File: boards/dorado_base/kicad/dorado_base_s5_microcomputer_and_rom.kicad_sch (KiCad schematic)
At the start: 11 parts

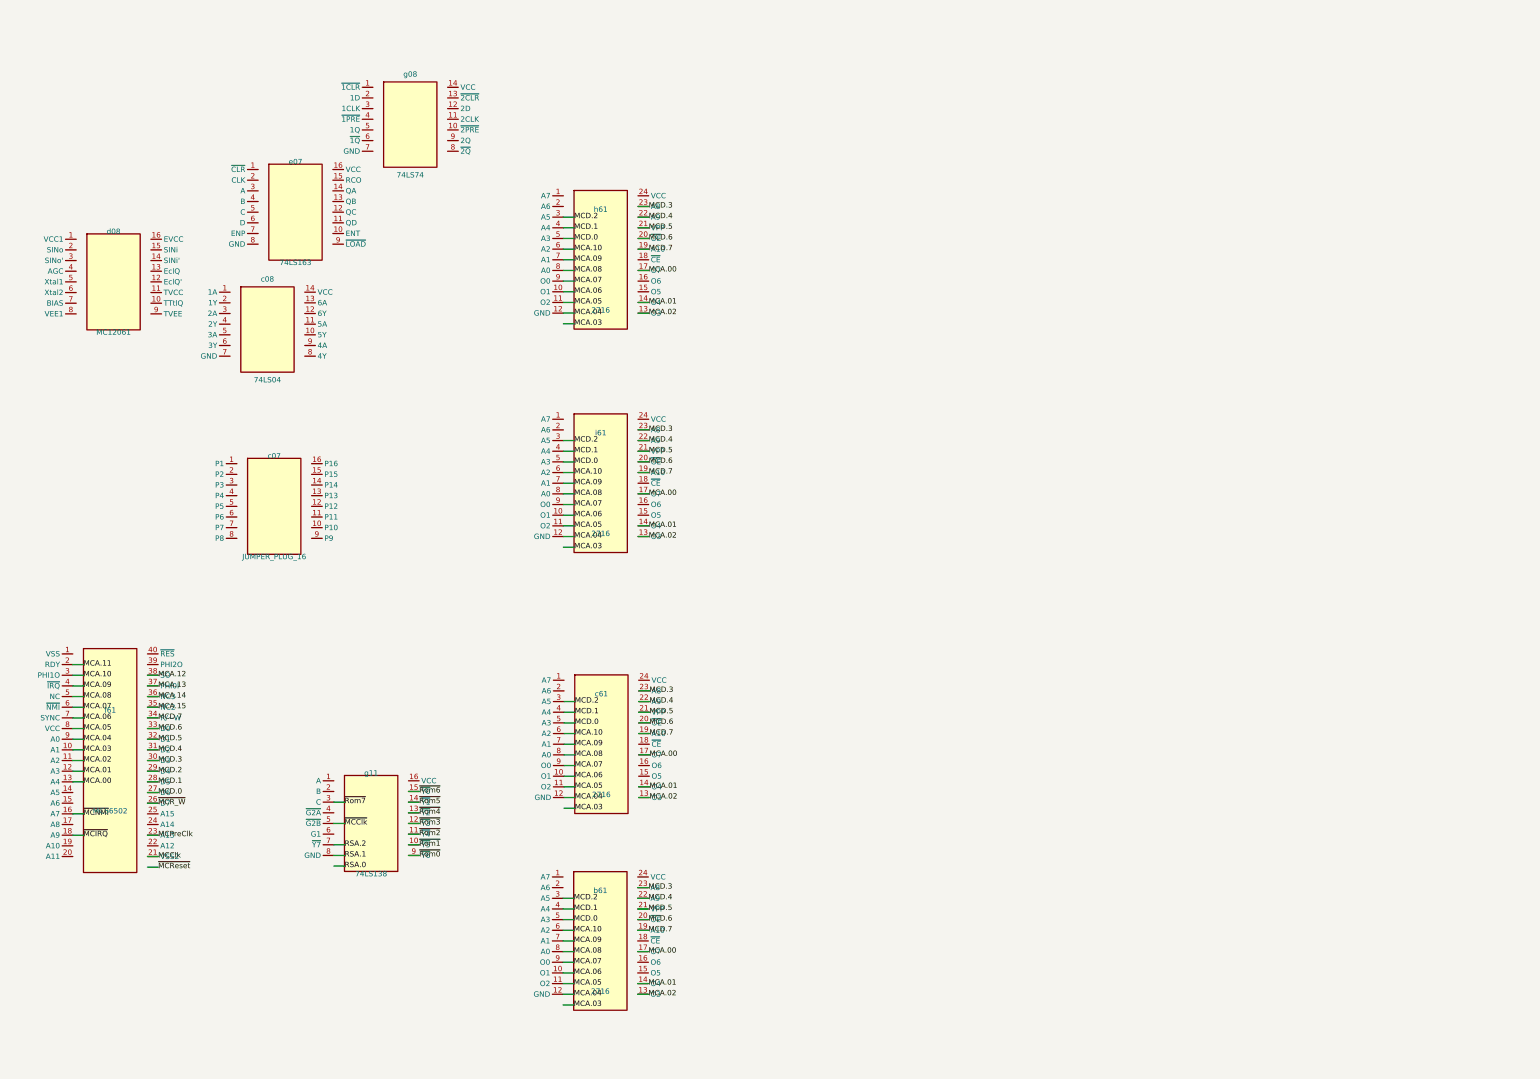
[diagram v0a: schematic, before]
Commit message: Harness improvements: split-gate exporter, extend-net, board ERC roll-up, on-demand PDF rendering
- kicad_export: emit per-sub-unit lib_symbols (e.g. MC10124_a/b/c/d) sized
  to each gate's pin set; sub-unit detection is graph-evidenced so chips
  with letter-named functional groups (74LS245 A/B) stay single-unit.
  Eliminates phantom pin_to_pin/multiple_net_names ERC errors on split-gate
  sheets and makes each gate render with only its own pins.

- explorer: defaultPinPositions filters to the active gate's pins for
  sub-unit refdes; mirrors kicad_export's predicate. getPinSourcePos now
  requires the component's sheet to match the current view, so endpoints
  with stale/missing sheet fields can't paint stray wires on undecoded
  pages. Also patched 11 such endpoints in dorado_base/graph.json.

- graph_cli: new extend-net verb appends endpoints to an existing net
  (errors on unknown net or edge_type mismatch, skips duplicates).
  erc-summary --board <id> aggregates every sheet's report and surfaces
  named labels with only one endpoint across the whole board — the real
  off-page connections still missing.

- cartographer: tile and crop-chip accept --pdf <path> --page <n>
  --dpi <n> to render fresh from the source PDF on demand. crop-chip
  auto-rescales the bbox by render-vs-scan size ratio so a 600 DPI crop
  still frames the chip from a graph populated against 300 DPI scans.

Co-Authored-By: Claude Opus 4.7 (1M context) <noreply@anthropic.com>
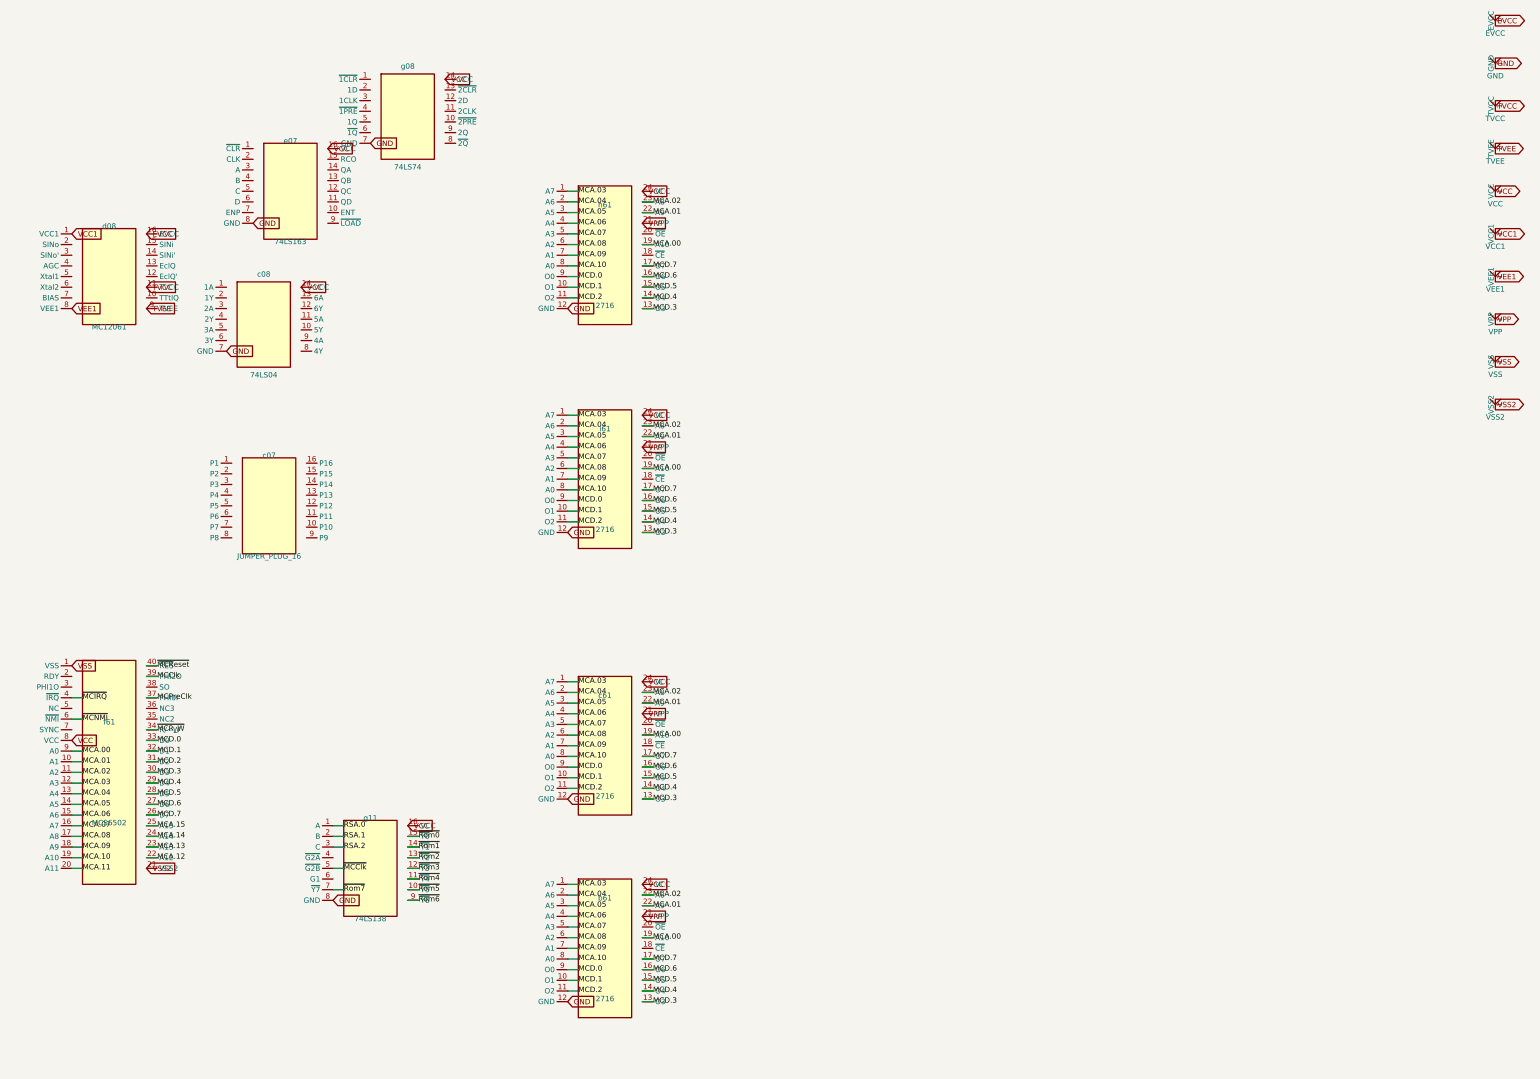
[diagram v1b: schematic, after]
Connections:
- net MCA.00: now also b61.19 (A10), c61.19 (A10), f61.9 (A0), h61.19 (A10), i61.19 (A10); no longer b61.17 (O7), c61.17 (O7), f61.13 (A4), h61.17 (O7), i61.17 (O7)
- net MCA.01: now also b61.22 (A9), c61.22 (A9), f61.10 (A1), h61.22 (A9), i61.22 (A9); no longer b61.14 (O4), c61.14 (O4), f61.12 (A3), h61.14 (O4), i61.14 (O4)
- net MCA.02: now also b61.23 (A8), c61.23 (A8), h61.23 (A8), i61.23 (A8); no longer b61.13 (O3), c61.13 (O3), h61.13 (O3), i61.13 (O3)
- net MCA.03: now also b61.1 (A7), c61.1 (A7), f61.12 (A3), h61.1 (A7), i61.1 (A7); no longer f61.10 (A1)
- net MCA.04: now also b61.2 (A6), c61.2 (A6), f61.13 (A4), h61.2 (A6), i61.2 (A6); no longer b61.12 (GND), c61.12 (GND), f61.9 (A0), h61.12 (GND), i61.12 (GND)
- net MCA.05: now also b61.3 (A5), c61.3 (A5), f61.14 (A5), h61.3 (A5), i61.3 (A5); no longer b61.11 (O2), c61.11 (O2), f61.8 (VCC), h61.11 (O2), i61.11 (O2)
- net MCA.06: now also b61.4 (A4), c61.4 (A4), f61.15 (A6), h61.4 (A4), i61.4 (A4); no longer b61.10 (O1), c61.10 (O1), f61.7 (SYNC), h61.10 (O1), i61.10 (O1)
- net MCA.07: now also b61.5 (A3), c61.5 (A3), f61.16 (A7), h61.5 (A3), i61.5 (A3); no longer b61.9 (O0), c61.9 (O0), f61.6 (~{NMI}), h61.9 (O0), i61.9 (O0)
- net MCA.08: now also b61.6 (A2), c61.6 (A2), f61.17 (A8), h61.6 (A2), i61.6 (A2); no longer b61.8 (A0), c61.8 (A0), f61.5 (NC), h61.8 (A0), i61.8 (A0)
- net MCA.09: now also f61.18 (A9); no longer f61.4 (~{IRQ})
- net MCA.10: now also b61.8 (A0), c61.8 (A0), f61.19 (A10), h61.8 (A0), i61.8 (A0); no longer b61.6 (A2), c61.6 (A2), f61.3 (PHI1O), h61.6 (A2), i61.6 (A2)
- net MCA.11: now also f61.20 (A11); no longer f61.2 (RDY)
- net MCA.12: now also f61.22 (A12); no longer f61.38 (SO)
- net MCA.13: now also f61.23 (A13); no longer f61.37 (PHI0I)
- net MCA.14: now also f61.24 (A14); no longer f61.36 (NC3)
- net MCA.15: now also f61.25 (A15); no longer f61.35 (NC2)
- net MCClk: now also f61.39 (PHI2O); no longer f61.21 (VSS2)
- net MCD.0: now also b61.9 (O0), c61.9 (O0), f61.33 (D0), h61.9 (O0), i61.9 (O0); no longer b61.5 (A3), c61.5 (A3), f61.27 (D6), h61.5 (A3), i61.5 (A3)
- net MCD.1: now also b61.10 (O1), c61.10 (O1), f61.32 (D1), h61.10 (O1), i61.10 (O1); no longer b61.4 (A4), c61.4 (A4), f61.28 (D5), h61.4 (A4), i61.4 (A4)
- net MCD.2: now also b61.11 (O2), c61.11 (O2), f61.31 (D2), h61.11 (O2), i61.11 (O2); no longer b61.3 (A5), c61.3 (A5), f61.29 (D4), h61.3 (A5), i61.3 (A5)
- net MCD.3: now also b61.13 (O3), c61.13 (O3), h61.13 (O3), i61.13 (O3); no longer b61.23 (A8), c61.23 (A8), h61.23 (A8), i61.23 (A8)
- net MCD.4: now also b61.14 (O4), c61.14 (O4), f61.29 (D4), h61.14 (O4), i61.14 (O4); no longer b61.22 (A9), c61.22 (A9), f61.31 (D2), h61.22 (A9), i61.22 (A9)
- net MCD.5: now also b61.15 (O5), c61.15 (O5), f61.28 (D5), h61.15 (O5), i61.15 (O5); no longer b61.21 (VPP), c61.21 (VPP), f61.32 (D1), h61.21 (VPP), i61.21 (VPP)
- net MCD.6: now also b61.16 (O6), c61.16 (O6), f61.27 (D6), h61.16 (O6), i61.16 (O6); no longer b61.20 (~{OE}), c61.20 (~{OE}), f61.33 (D0), h61.20 (~{OE}), i61.20 (~{OE})
- net MCD.7: now also b61.17 (O7), c61.17 (O7), f61.26 (D7), h61.17 (O7), i61.17 (O7); no longer b61.19 (A10), c61.19 (A10), f61.34 (R/~W), h61.19 (A10), i61.19 (A10)
- net MCPreClk: now also f61.37 (PHI0I); no longer f61.23 (A13)
- net RSA.0: now also g11.1 (A)
- net RSA.1: now also g11.2 (B); no longer g11.8 (GND)
- net RSA.2: now also g11.3 (C); no longer g11.7 (~{Y7})
- net ~{MCIRQ}: now also f61.4 (~{IRQ}); no longer f61.18 (A9)
- net ~{MCNMI}: now also f61.6 (~{NMI}); no longer f61.16 (A7)
- net ~{MCR_W}: now also f61.34 (R/~W); no longer f61.26 (D7)
- net ~{MCReset}: now also f61.40 (~{RES})
- net ~{Rom0}: now also g11.15 (~{Y0}); no longer g11.9 (~{Y6})
- net ~{Rom1}: now also g11.14 (~{Y1}); no longer g11.10 (~{Y5})
- net ~{Rom2}: now also g11.13 (~{Y2}); no longer g11.11 (~{Y4})
- net ~{Rom4}: now also g11.11 (~{Y4}); no longer g11.13 (~{Y2})
- net ~{Rom5}: now also g11.10 (~{Y5}); no longer g11.14 (~{Y1})
- net ~{Rom6}: now also g11.9 (~{Y6}); no longer g11.15 (~{Y0})
- net ~{Rom7}: now also g11.7 (~{Y7}); no longer g11.3 (C)
- net VCC: now reaches g08.14 (VCC)
- net VCC: now also b61.24 (VCC), c08.14 (VCC), c61.24 (VCC), e07.16 (VCC), f61.8 (VCC), g11.16 (VCC), h61.24 (VCC), i61.24 (VCC)
- net GND: now reaches g08.7 (GND)
- net GND: now also b61.12 (GND), c08.7 (GND), c61.12 (GND), e07.8 (GND), g11.8 (GND), h61.12 (GND), i61.12 (GND)
- net VCC1: now reaches d08.1 (VCC1)
- net TVCC: now reaches d08.11 (TVCC)
- net EVCC: now reaches d08.16 (EVCC)
- net VEE1: now reaches d08.8 (VEE1)
- net TVEE: now reaches d08.9 (TVEE)
- net VSS: now reaches f61.1 (VSS)
- new net VPP: b61.21 (VPP), c61.21 (VPP), h61.21 (VPP), i61.21 (VPP)
- new net VSS2: f61.21 (VSS2)
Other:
- moved on the sheet: b61, c07, c08, c61, d08, e07, f61, g08, g11, h61, i61

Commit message: kicad export: faithful per-component symbols + path-aware wire routing
Switches the exporter from generic DIP symbols + straight-line pin-to-pin
wires to a per-component lib_symbol whose body matches the source bbox
and whose pins land at the placed pin_positions. The KiCad-rendered
schematic now reflects the original drawing's chip layout instead of an
auto-laid-out re-draw.

- synth_faithful_symbol(refdes, part, comp, scale): emits a unique
  user:_chip_<refdes> lib_symbol per component. Body shrunk by PIN_LENGTH
  on each side so pin lines extend visibly to the schematic dot. Pin
  (at) coords snapped to the 50-mil grid; angle picked from which body
  edge the pin is closest to.
- gen_sch chooses faithful when the component has pin_positions, else
  falls back to the existing generic synth_symbol path (so partly-
  transcribed sheets still export). pin_endpoint_mm in the faithful
  branch uses snapped local offsets so the absolute pin position equals
  instance_origin + offset, both grid-aligned (clears endpoint_off_grid).
- Wire emission: when net.path is set, emit one (wire) per consecutive
  polyline pair, snapped to grid. When absent, fall back to a one-corner
  Manhattan H-then-V route between each endpoint pair instead of a
  diagonal — gives KiCad something loadable until the tracer fills paths
  in. (Net path is consumed end-to-end through (wire (pts ...)).)
- Junctions: per-sheet sheets[].junctions emit (junction (at x y))
  blocks so KiCad's renderer draws connection dots where two wires
  cross AND connect.

Sheet 5 (full pin_positions, no split-gates) goes from
"blocking(35): endpoint_off_grid=11, power_pin_not_driven=24" to
PASS — only cross-sheet noise remains. Sheets 7 and 8 stay blocking=0
with their pre-existing pin_to_pin graph bugs unchanged.

Co-Authored-By: Claude Opus 4.7 (1M context) <noreply@anthropic.com>
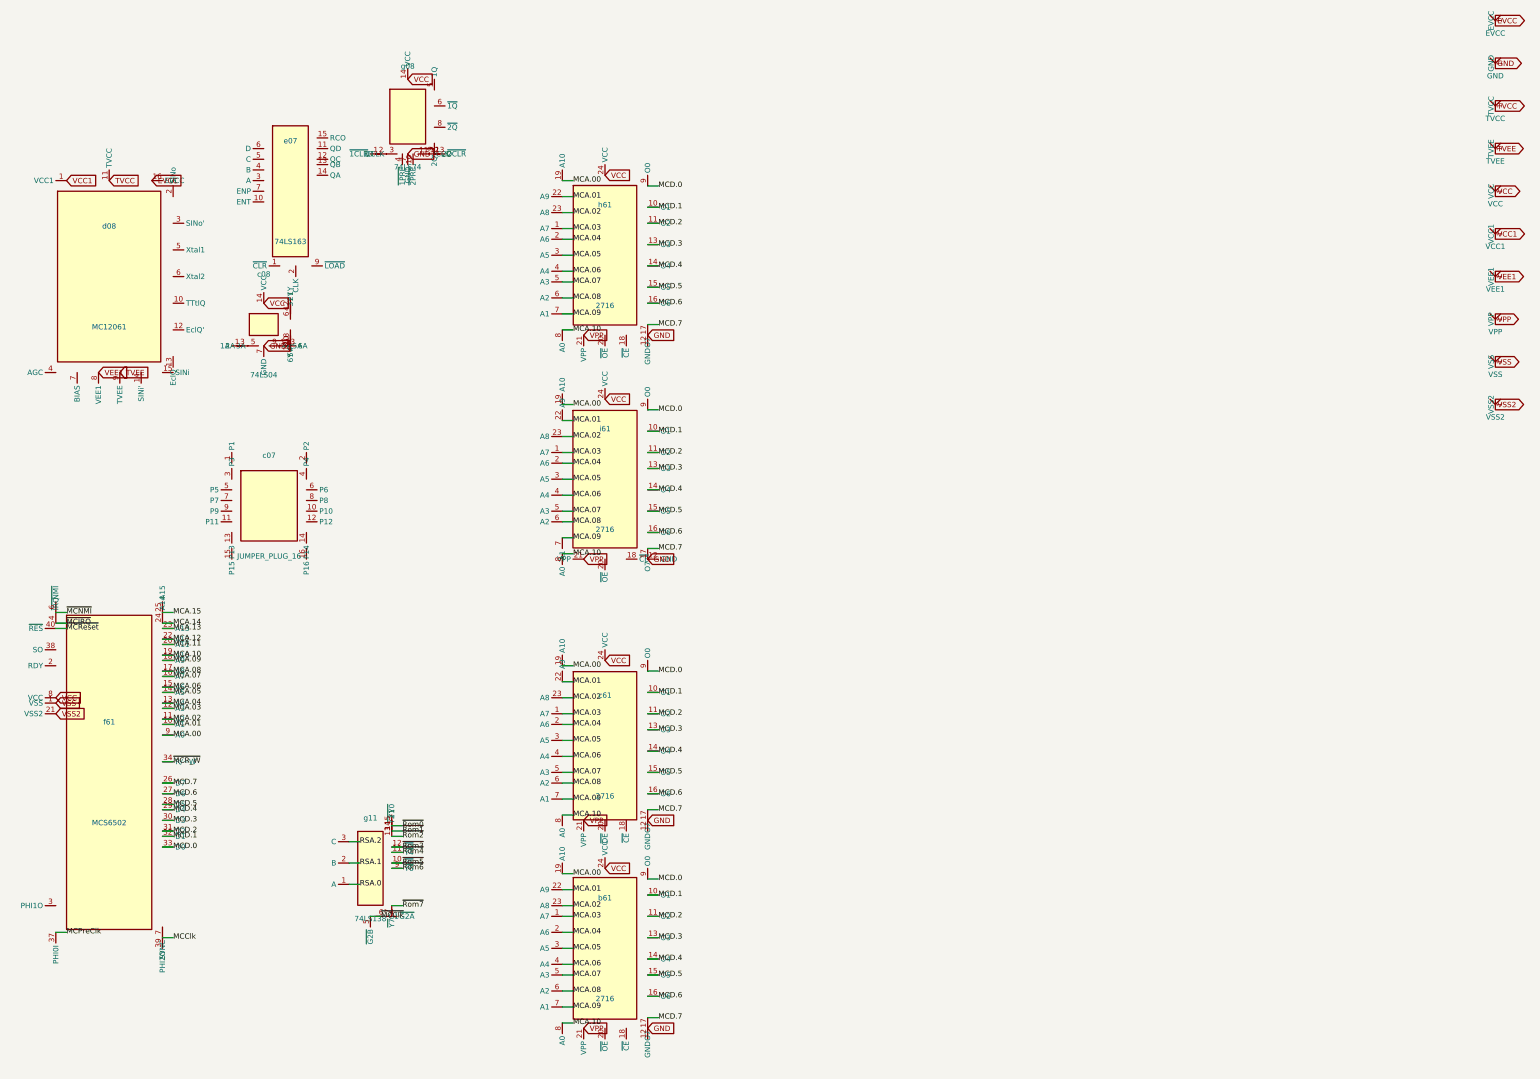
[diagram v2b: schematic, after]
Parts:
- b61: symbol user:2716 -> user:_chip_b61
- c07: symbol user:JUMPER_PLUG_16 -> user:_chip_c07
- c08: symbol user:74LS04 -> user:_chip_c08
- c61: symbol user:2716 -> user:_chip_c61
- d08: symbol user:MC12061 -> user:_chip_d08
- e07: symbol user:74LS163 -> user:_chip_e07
- f61: symbol user:MCS6502 -> user:_chip_f61
- g08: symbol user:74LS74 -> user:_chip_g08
- g11: symbol user:74LS138 -> user:_chip_g11
- h61: symbol user:2716 -> user:_chip_h61
- i61: symbol user:2716 -> user:_chip_i61
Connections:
- net GND: no longer e07.8 (GND), g11.8 (GND)
- net VCC: no longer e07.16 (VCC), g11.16 (VCC)
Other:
- moved on the sheet: b61, c07, c08, c61, d08, g08, h61, i61
